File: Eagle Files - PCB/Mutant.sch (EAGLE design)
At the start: 28 parts, among them M1 ARDUINO-NANO-3.0

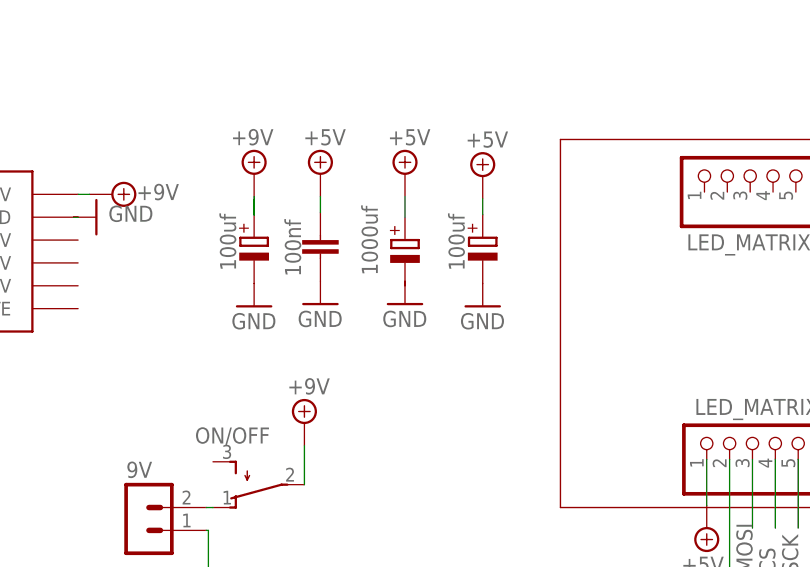
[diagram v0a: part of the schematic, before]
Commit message: Code updated - Define buttons for rec and retrig swapped
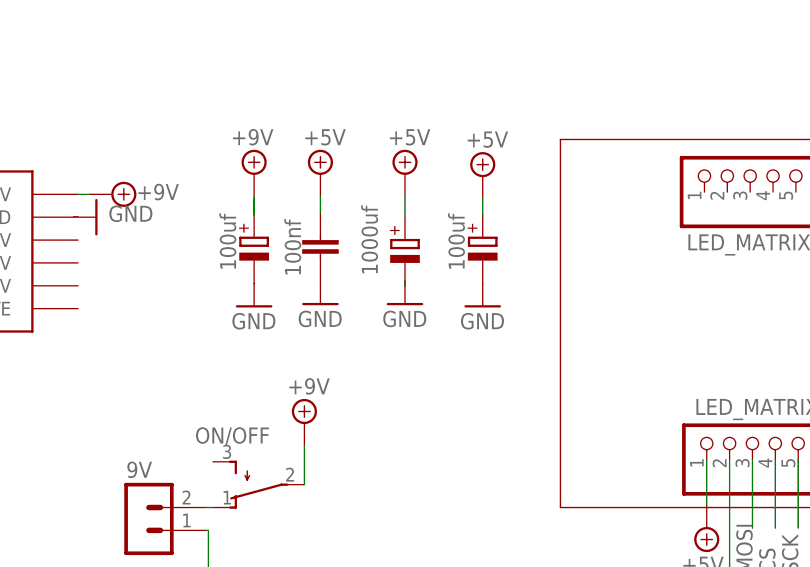
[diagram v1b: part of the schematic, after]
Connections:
- net GND: now also C5.-
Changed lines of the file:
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@@
 <pinref part="C3" gate="G$1" pin="-"/>
+</segment>
+<segment>
+<pinref part="C5" gate="G$1" pin="-"/>
+<pinref part="GND15" gate="1" pin="GND"/>
+<wire x1="30.48" y1="71.12" x2="30.48" y2="71.628" width="0.1524" layer="91"/>
 </segment>
 </net>
